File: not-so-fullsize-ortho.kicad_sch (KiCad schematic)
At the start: 10 parts, among them J3 Conn_01x03, J4 Conn_01x04

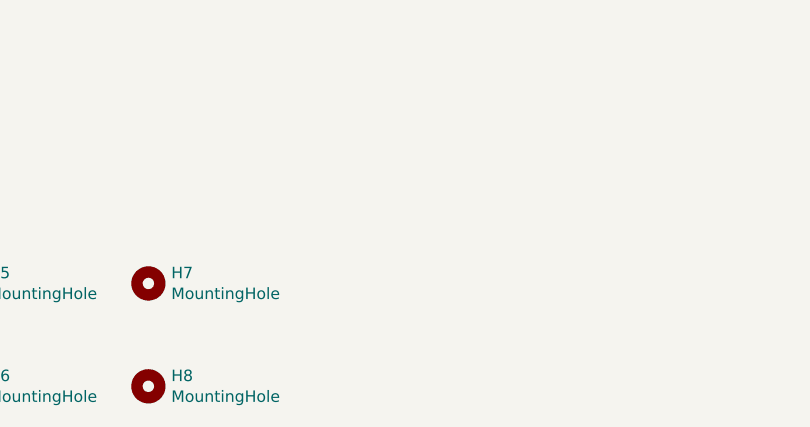
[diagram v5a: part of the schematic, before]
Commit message: test prod files for jlc quote, wrong diode footprint 🤦‍
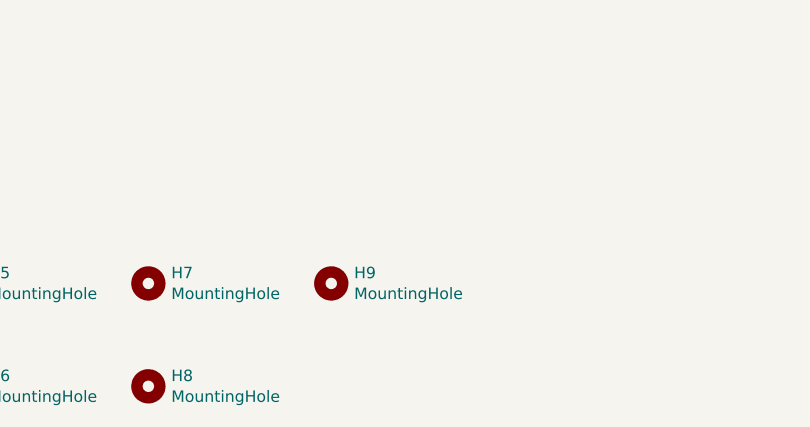
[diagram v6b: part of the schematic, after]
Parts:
- added H9: MountingHole, MountingHole:MountingHole_2.2mm_M2, symbol Mechanical:MountingHole
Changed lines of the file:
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@@
+	(symbol
+		(lib_id "Mechanical:MountingHole")
+		(at 101.6 267.97 0)
+		(unit 1)
+		(exclude_from_sim no)
+		(in_bom yes)
+		(on_board yes)
+		(dnp no)
+		(property "Reference" "H9"
+			(at 104.14 266.8016 0)
+			(effects
+				(font
+					(size 1.27 1.27)
+				)
+				(justify left)
+			)
+		)
+		(property "Value" "MountingHole"
+			(at 104.14 269.113 0)
+			(effects
+				(font
+					(size 1.27 1.27)
+				)
+				(justify left)
+			)
+		)
+		(property "Footprint" "MountingHole:MountingHole_2.2mm_M2"
+			(at 101.6 267.97 0)
+			(effects
+				(font
+					(size 1.27 1.27)
+				)
+				(hide yes)
+			)
+		)
+		(property "Datasheet" "~"
+			(at 101.6 267.97 0)
+			(effects
+				(font
+					(size 1.27 1.27)
+				)
+				(hide yes)
+			)
+		)
+		(property "Description" ""
+			(at 101.6 267.97 0)
+			(effects
+				(font
+					(size 1.27 1.27)
+				)
+				(hide yes)
+			)
+		)
+		(instances
+			(project "not-so-fullsize-ortho"
+				(path "/e63e39d7-6ac0-4ffd-8aa3-1841a4541b55"
+					(reference "H9")
+					(unit 1)
+				)
+			)
+		)
+	)
 	(symbol
 		(lib_id "Mechanical:MountingHole")
